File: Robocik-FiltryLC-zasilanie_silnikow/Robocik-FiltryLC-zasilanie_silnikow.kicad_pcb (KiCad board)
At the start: 2 copper layers, 160 x 130 mm, 18 parts, among them J1 XT90PW-F, J2 Conn_01x05, J3 Conn_01x03, J4 Conn_01x03, J5 Conn_01x03, J6 Conn_01x03, U1 ESC, U2 ESC, U3 ESC, U4 ESC

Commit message: Added second board. Added 3D models to most elements. Included PCB top and botton jpg files. Resized PCB - from 12 x 17 cm to 10,5 x 12,5cm.
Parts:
- added C5: CP, Capacitor_THT:C_Radial_D10.0mm_H20.0mm_P5.00mm, F.Cu at (273.4, 55.7)
- added C6: CP, Capacitor_THT:C_Radial_D10.0mm_H20.0mm_P5.00mm, F.Cu at (273.4, 34.7)
- added C7: CP, Capacitor_THT:C_Radial_D10.0mm_H20.0mm_P5.00mm, F.Cu at (273.4, 76.7)
- added C8: CP, Capacitor_THT:C_Radial_D10.0mm_H20.0mm_P5.00mm, F.Cu at (273.4, 97.7)
- added J10: Conn_01x03, Connectors:MR30PW-FB, F.Cu at (197.3, 76.7)
- added J11: Conn_01x03, Connectors:MR30PW-FB, F.Cu at (197.3, 97.7)
- added J12: Conn_01x05, Connector_Molex:Molex_SPOX_5267-05A_1x05_P2.50mm_Vertical, F.Cu at (251.7, 112.4)
- added J7: XT90PW-F, Connectors:XT90PW-F, F.Cu at (272.1, 112.9)
- added J8: Conn_01x03, Connectors:MR30PW-FB, F.Cu at (197.3, 55.7)
- added J9: Conn_01x03, Connectors:MR30PW-FB, F.Cu at (197.3, 34.7)
- added L5: L, 74435571100:WE-HCI_189023, F.Cu at (298.9, 55.7)
- added L6: L, 74435571100:WE-HCI_189023, F.Cu at (298.9, 34.7)
- added L7: L, 74435571100:WE-HCI_189023, F.Cu at (298.9, 76.7)
- added L8: L, 74435571100:WE-HCI_189023, F.Cu at (298.9, 97.7)
- added U5: ESC, ESC:ESC, F.Cu at (229.8, 55.7)
- added U6: ESC, ESC:ESC, F.Cu at (229.8, 34.7)
- added U7: ESC, ESC:ESC, F.Cu at (229.8, 76.7)
- added U8: ESC, ESC:ESC, F.Cu at (229.8, 97.7)
- moved J3 40.4 mm to (149.3, 55.7)
- moved J1 39.1 mm to (75.4, 112.9)
- moved J2 37.0 mm to (104.8, 111.6), turned to 180 degrees
- moved U1 36.8 mm to (116.8, 55.7)
- moved J5 30.8 mm to (149.3, 76.7)
- moved J4 30.1 mm to (149.3, 97.7)
- moved J6 26.2 mm to (149.3, 34.7)
- moved U3 25.9 mm to (116.8, 76.7)
- moved U2 25.0 mm to (116.8, 97.7)
- moved U4 20.2 mm to (116.8, 34.7)
- moved C2 10.3 mm to (73.5, 97.7)
- moved L2 10.3 mm to (48.5, 97.7)
- moved C4 6.20 mm to (73.5, 34.7)
- moved L4 6.20 mm to (48.5, 34.7)
- moved C3 4.80 mm to (73.5, 76.7)
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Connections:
- J1 pad 1: Net-(J1-Pad1) -> GND
- J1 pad 2: GND -> Net-(J1-Pad2)
- J3 pad 4: GND -> (no net)
- J3 pad 5: GND -> (no net)
- J4 pad 4: GND -> (no net)
- J4 pad 5: GND -> (no net)
- J5 pad 4: GND -> (no net)
- J5 pad 5: GND -> (no net)
- J6 pad 4: GND -> (no net)
- J6 pad 5: GND -> (no net)
- L1 pad 1: Net-(J1-Pad1) -> Net-(J1-Pad2)
- L2 pad 1: Net-(J1-Pad1) -> Net-(J1-Pad2)
- L3 pad 1: Net-(J1-Pad1) -> Net-(J1-Pad2)
- L4 pad 1: Net-(J1-Pad1) -> Net-(J1-Pad2)
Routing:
- net Net-(J1-Pad2): track 0.00 -> 152.8 mm, vias 0 -> 4
- net Net-(J7-Pad2): track 0.00 -> 140.1 mm, vias 0 -> 4
- net Net-(J1-Pad1): track 130.4 -> 0.00 mm, vias 4 -> 0
- net Net-(C8-Pad1): track 0.00 -> 18.9 mm, vias 0 -> 1
- net Net-(C7-Pad1): track 0.00 -> 18.9 mm, vias 0 -> 1
- net Net-(C6-Pad1): track 0.00 -> 18.9 mm, vias 0 -> 1
- net Net-(C5-Pad1): track 0.00 -> 18.9 mm, vias 0 -> 1
- net Net-(C4-Pad1): track 6.85 -> 18.4 mm
- net Net-(C3-Pad1): track 6.85 -> 18.4 mm
- net Net-(C1-Pad1): track 6.85 -> 18.4 mm
- net Net-(C2-Pad1): track 7.35 -> 18.4 mm
- removed copper zone on B.Cu, net Net-(C1-Pad1)
- removed copper zone on B.Cu, net Net-(C2-Pad1)
- removed copper zone on B.Cu, net Net-(C3-Pad1)
- removed copper zone on B.Cu, net Net-(C4-Pad1)
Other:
- board size 160 x 130 mm -> 286.6 x 104 mm

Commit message: Moved power connector to the side of the board. Added wiring for ESC output. Removed soldermask layers from high power lines.
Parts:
- moved J1 48.7 mm to (27.7, 103.2), turned to 270 degrees
- moved J7 47.9 mm to (319.0, 103.1), turned to 90 degrees
- moved J12 6.14 mm to (245.7, 111.1)
- moved J2 6.02 mm to (110.8, 111.1)
- moved L5 0.80 mm to (298.1, 55.7)
- moved L6 0.80 mm to (298.1, 34.7)
- moved L7 0.80 mm to (298.1, 76.7)
- moved L8 0.80 mm to (298.1, 97.7)
- moved C5 0.30 mm to (273.1, 55.7)
- moved C6 0.30 mm to (273.1, 34.7)
- moved C7 0.30 mm to (273.1, 76.7)
- moved C8 0.30 mm to (273.1, 97.7)
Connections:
- J1 pad 1: GND -> Net-(J1-Pad1)
- J1 pad 2: Net-(J1-Pad2) -> GND
- J12 pad 4: Net-(J12-Pad4) -> Net-(J12-Pad5)
- J12 pad 5: Net-(J12-Pad5) -> Net-(J12-Pad4)
- J2 pad 3: Net-(J2-Pad3) -> Net-(J2-Pad5)
- J2 pad 4: Net-(J2-Pad4) -> Net-(J2-Pad3)
- J2 pad 5: Net-(J2-Pad5) -> Net-(J2-Pad4)
- L1 pad 1: Net-(J1-Pad2) -> Net-(J1-Pad1)
- L2 pad 1: Net-(J1-Pad2) -> Net-(J1-Pad1)
- L3 pad 1: Net-(J1-Pad2) -> Net-(J1-Pad1)
- L4 pad 1: Net-(J1-Pad2) -> Net-(J1-Pad1)
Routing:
- net Net-(J1-Pad2): track 152.8 -> 0.00 mm, vias 4 -> 0
- net Net-(J1-Pad1): track 0.00 -> 98.7 mm, vias 0 -> 4
- net Net-(J2-Pad2): track 0.00 -> 81.9 mm
- net Net-(J12-Pad4): track 0.00 -> 80.3 mm
- net Net-(J2-Pad5): track 0.00 -> 59.8 mm
- net Net-(J12-Pad5): track 0.00 -> 58.3 mm
- net Net-(J7-Pad2): track 140.1 -> 96.5 mm
- net Net-(J2-Pad3): track 0.00 -> 38.1 mm
- net Net-(J12-Pad3): track 0.00 -> 36.2 mm
- net Net-(J11-Pad3): track 0.00 -> 32.9 mm
- net Net-(J11-Pad1): track 0.00 -> 32.7 mm
- net Net-(J11-Pad2): track 0.00 -> 30.3 mm
- net Net-(J5-Pad3): track 0.00 -> 22.0 mm
- net Net-(J4-Pad3): track 0.00 -> 22.0 mm
- net Net-(J6-Pad3): track 0.00 -> 22.0 mm
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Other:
- board size 286.6 x 104 mm -> 314.6 x 92.7 mm

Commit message: Added mounting screws for bus bars. Increased size of power+ bus bar copper layer.
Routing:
- net Net-(J1-Pad1): track 98.7 -> 271.6 mm, vias 4 -> 7
- net Net-(J7-Pad2): track 96.5 -> 252.9 mm, vias 4 -> 7
- net GND: track 2.11 -> 34.3 mm, vias 0 -> 10

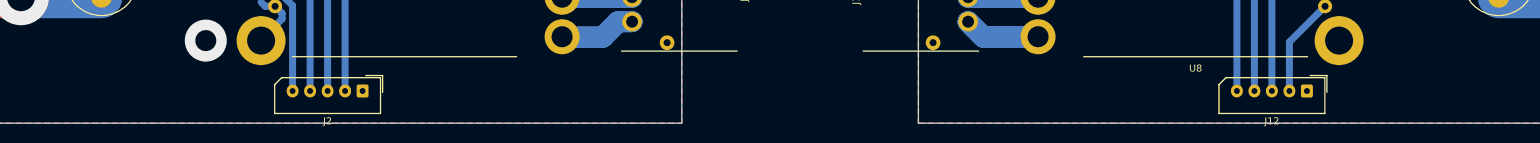
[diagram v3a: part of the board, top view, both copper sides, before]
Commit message: Addeed additional mounting screws for bus bars.
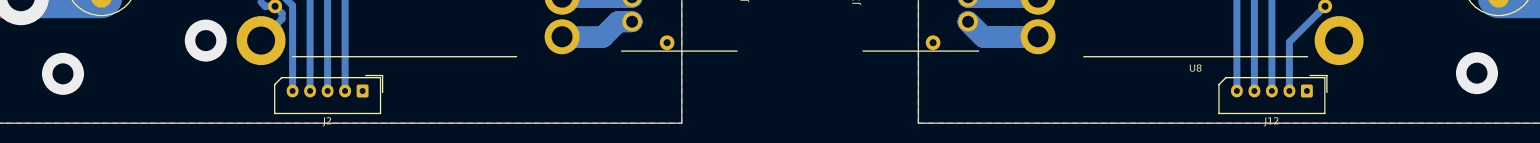
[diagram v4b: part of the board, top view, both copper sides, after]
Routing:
- net GND: vias 10 -> 12
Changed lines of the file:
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@@
     (thickness 1.6)
     (drawings 45)
-    (tracks 225)
+    (tracks 227)
     (zones 0)
     (modules 36)
@@
   (via (at 88.4 61.9) (size 6) (drill 3) (layers F.Cu B.Cu) (net 1))
   (via (at 88.4 40.9) (size 6) (drill 3) (layers F.Cu B.Cu) (net 1))
+  (via (at 270 108.55) (size 6) (drill 3) (layers F.Cu B.Cu) (net 1))
+  (via (at 68 108.65) (size 6) (drill 3) (layers F.Cu B.Cu) (net 1))
   (via (at 62 55.7) (size 8) (drill 4) (layers F.Cu B.Cu) (net 2))
   (segment (start 55.15 55.7) (end 62 55.7) (width 6) (layer F.Cu) (net 2))

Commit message: Added connector and PCB labels on board.
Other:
- board text added: "BLDC driver PCB v1"
- board text added: "Engines OUT"
- board text added: "PWM signals"
- board text added: "Power Supply 16V"
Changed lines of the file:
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@@
   (general
     (thickness 1.6)
-    (drawings 45)
+    (drawings 53)
     (tracks 227)
     (zones 0)
@@
     )
   )
+  (gr_text "BLDC driver PCB v1\n" (at 327.9 36.2 90) (layer F.SilkS)
+    (effects (font (size 1.5 1.5) (thickness 0.3)))
+  )
+  (gr_text "BLDC driver PCB v1\n" (at 19.2 36.2 270) (layer F.SilkS)
+    (effects (font (size 1.5 1.5) (thickness 0.3)))
+  )
+  (gr_text "Power Supply 16V" (at 327.7 81.2 90) (layer F.SilkS)
+    (effects (font (size 1.5 1.5) (thickness 0.3)))
+  )
+  (gr_text "PWM signals" (at 224.7 111.6) (layer F.SilkS)
+    (effects (font (size 1.5 1.5) (thickness 0.3)))
+  )
+  (gr_text "Engines OUT" (at 198.4 111.6) (layer F.SilkS)
+    (effects (font (size 1.5 1.5) (thickness 0.3)))
+  )
+  (gr_text "Engines OUT" (at 148.6 111.7) (layer F.SilkS)
+    (effects (font (size 1.5 1.5) (thickness 0.3)))
+  )
+  (gr_text "PWM signals" (at 121.3 111.6) (layer F.SilkS)
+    (effects (font (size 1.5 1.5) (thickness 0.3)))
+  )
+  (gr_text "Power Supply 16V" (at 19.2 81.2 270) (layer F.SilkS)
+    (effects (font (size 1.5 1.5) (thickness 0.3)))
+  )
   (gr_poly (pts (xy 311.8 31.7) (xy 311.4 31.7) (xy 310.5 32) (xy 309.7 32.6) (xy 309.2 33.3) (xy 308.9 34.2) (xy 308.9 34.9) (xy 309 97.8) (xy 309 98.2) (xy 309.2 99) (xy 309.9 100) (xy 311 100.6) (xy 311.6 100.7) (xy 320.7 100.7) (xy 321.5 100.1) (xy 322.3 98.4) (xy 322.2 96.9) (xy 322 95.9) (xy 322 34.3) (xy 321.8 33.5) (xy 321.4 32.8) (xy 320.5 32) (xy 319.5 31.7)) (layer B.Mask) (width 0.1))
